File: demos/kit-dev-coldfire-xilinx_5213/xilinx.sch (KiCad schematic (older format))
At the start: 21 parts, among them P1 CONN_6, P3 CONN_2X2, P4 CONN_20X2, U9 XCR3256-TQ144

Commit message: 3d viewer: minor code cleaning (remove useless #include ) dialog_track_via_size: set minimal size  and make dialog resizable. Update demo file.
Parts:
- C51, C52, C53, C54, C55, C56, C57, C58, C59, C60, C61, R57, R62, R63: footprint (none) -> lib_smd:SM0805
- D8, D9: footprint (none) -> lib_smd:SM1206POL
- P1: footprint (none) -> pin_array:PIN_ARRAY-6X1
- P3: footprint (none) -> pin_array:PIN_ARRAY_2X2
- P4: footprint (none) -> pin_array:PIN_ARRAY_20X2
- R64: footprint (none) -> discret:R4
- U9: footprint (none) -> lib_smd:TQFP144
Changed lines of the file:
@@
 F 0 "R64" V 10530 3900 50  0000 C CNN
 F 1 "3,3" V 10450 3900 50  0000 C CNN
-F 2 "" H 10450 3900 60  0001 C CNN
+F 2 "discret:R4" H 10450 3900 60  0001 C CNN
 F 3 "" H 10450 3900 60  0001 C CNN
 	1    10450 3900
@@
 F 0 "P3" H 6600 1400 50  0000 C CNN
 F 1 "CONN_2X2" H 6610 1120 40  0000 C CNN
-F 2 "" H 6600 1250 60  0001 C CNN
+F 2 "pin_array:PIN_ARRAY_2X2" H 6600 1250 60  0001 C CNN
 F 3 "" H 6600 1250 60  0001 C CNN
 	1    6600 1250
@@
 F 0 "U9" H 4600 4150 70  0000 C CNN
 F 1 "XCR3256-TQ144" H 4550 500 60  0000 C CNN
-F 2 "" H 4550 4100 60  0001 C CNN
+F 2 "lib_smd:TQFP144" H 4550 4100 60  0001 C CNN
 F 3 "" H 4550 4100 60  0001 C CNN
 	1    4550 4100
@@
 F 0 "P4" H 9250 3100 60  0000 C CNN
 F 1 "CONN_20X2" V 9200 3050 50  0000 C CNN
-F 2 "" H 9200 3050 60  0001 C CNN
+F 2 "pin_array:PIN_ARRAY_20X2" H 9200 3050 60  0001 C CNN
 F 3 "" H 9200 3050 60  0001 C CNN
 	1    9200 3050
@@
 F 0 "R57" V 3380 650 50  0000 C CNN
 F 1 "4K7" V 3300 650 50  0000 C CNN
-F 2 "" H 3300 650 60  0001 C CNN
+F 2 "lib_smd:SM0805" H 3300 650 60  0001 C CNN
 F 3 "" H 3300 650 60  0001 C CNN
 	1    3300 650
@@
 F 0 "D8" H 9300 5050 50  0000 C CNN
 F 1 "LED" H 9300 4850 50  0000 C CNN
-F 2 "" H 9300 4950 60  0001 C CNN
+F 2 "lib_smd:SM1206POL" H 9300 4950 60  0001 C CNN
 F 3 "" H 9300 4950 60  0001 C CNN
 	1    9300 4950
@@
 F 0 "R62" V 8880 4950 50  0000 C CNN
 F 1 "1K" V 8800 4950 50  0000 C CNN
-F 2 "" H 8800 4950 60  0001 C CNN
+F 2 "lib_smd:SM0805" H 8800 4950 60  0001 C CNN
 F 3 "" H 8800 4950 60  0001 C CNN
 	1    8800 4950
@@
 F 0 "C61" H 10700 6450 50  0000 L CNN
 F 1 "100nF" H 10650 6250 50  0000 L CNN
-F 2 "" H 10650 6350 60  0001 C CNN
+F 2 "lib_smd:SM0805" H 10650 6350 60  0001 C CNN
 F 3 "" H 10650 6350 60  0001 C CNN
 	1    10650 6350
@@
 F 0 "C60" H 10400 6450 50  0000 L CNN
 F 1 "100nF" H 10350 6250 50  0000 L CNN
-F 2 "" H 10350 6350 60  0001 C CNN
+F 2 "lib_smd:SM0805" H 10350 6350 60  0001 C CNN
 F 3 "" H 10350 6350 60  0001 C CNN
 	1    10350 6350
@@
 F 0 "C59" H 10100 6450 50  0000 L CNN
 F 1 "100nF" H 10050 6250 50  0000 L CNN
-F 2 "" H 10050 6350 60  0001 C CNN
+F 2 "lib_smd:SM0805" H 10050 6350 60  0001 C CNN
 F 3 "" H 10050 6350 60  0001 C CNN
 	1    10050 6350
@@
 F 0 "C54" H 8600 6450 50  0000 L CNN
 F 1 "100nF" H 8550 6250 50  0000 L CNN
-F 2 "" H 8550 6350 60  0001 C CNN
+F 2 "lib_smd:SM0805" H 8550 6350 60  0001 C CNN
 F 3 "" H 8550 6350 60  0001 C CNN
 	1    8550 6350
@@
 F 0 "C53" H 8300 6450 50  0000 L CNN
 F 1 "100nF" H 8250 6250 50  0000 L CNN
-F 2 "" H 8250 6350 60  0001 C CNN
+F 2 "lib_smd:SM0805" H 8250 6350 60  0001 C CNN
 F 3 "" H 8250 6350 60  0001 C CNN
 	1    8250 6350
@@
 F 0 "C52" H 8000 6450 50  0000 L CNN
 F 1 "100nF" H 7950 6250 50  0000 L CNN
-F 2 "" H 7950 6350 60  0001 C CNN
+F 2 "lib_smd:SM0805" H 7950 6350 60  0001 C CNN
 F 3 "" H 7950 6350 60  0001 C CNN
 	1    7950 6350
@@
 F 0 "C51" H 7700 6450 50  0000 L CNN
 F 1 "100nF" H 7650 6250 50  0000 L CNN
-F 2 "" H 7650 6350 60  0001 C CNN
+F 2 "lib_smd:SM0805" H 7650 6350 60  0001 C CNN
 F 3 "" H 7650 6350 60  0001 C CNN
 	1    7650 6350
@@
 F 0 "C58" H 9800 6450 50  0000 L CNN
 F 1 "100nF" H 9750 6250 50  0000 L CNN
-F 2 "" H 9750 6350 60  0001 C CNN
+F 2 "lib_smd:SM0805" H 9750 6350 60  0001 C CNN
 F 3 "" H 9750 6350 60  0001 C CNN
 	1    9750 6350
@@
 F 0 "C57" H 9500 6450 50  0000 L CNN
 F 1 "100nF" H 9450 6250 50  0000 L CNN
-F 2 "" H 9450 6350 60  0001 C CNN
+F 2 "lib_smd:SM0805" H 9450 6350 60  0001 C CNN
 F 3 "" H 9450 6350 60  0001 C CNN
 	1    9450 6350
@@
 F 0 "C56" H 9200 6450 50  0000 L CNN
 F 1 "100nF" H 9150 6250 50  0000 L CNN
-F 2 "" H 9150 6350 60  0001 C CNN
+F 2 "lib_smd:SM0805" H 9150 6350 60  0001 C CNN
 F 3 "" H 9150 6350 60  0001 C CNN
 	1    9150 6350
@@
 F 0 "C55" H 8900 6450 50  0000 L CNN
 F 1 "100nF" H 8850 6250 50  0000 L CNN
-F 2 "" H 8850 6350 60  0001 C CNN
+F 2 "lib_smd:SM0805" H 8850 6350 60  0001 C CNN
 F 3 "" H 8850 6350 60  0001 C CNN
 	1    8850 6350
@@
 F 0 "D9" H 9300 5350 50  0000 C CNN
 F 1 "LED" H 9300 5150 50  0000 C CNN
-F 2 "" H 9300 5250 60  0001 C CNN
+F 2 "lib_smd:SM1206POL" H 9300 5250 60  0001 C CNN
 F 3 "" H 9300 5250 60  0001 C CNN
 	1    9300 5250
@@
 F 0 "R63" V 8880 5250 50  0000 C CNN
 F 1 "1K" V 8800 5250 50  0000 C CNN
-F 2 "" H 8800 5250 60  0001 C CNN
+F 2 "lib_smd:SM0805" H 8800 5250 60  0001 C CNN
 F 3 "" H 8800 5250 60  0001 C CNN
 	1    8800 5250
@@
 F 0 "P1" V 2300 1050 60  0000 C CNN
 F 1 "CONN_6" V 2400 1050 60  0000 C CNN
-F 2 "" H 2350 1050 60  0001 C CNN
+F 2 "pin_array:PIN_ARRAY-6X1" H 2350 1050 60  0001 C CNN
 F 3 "" H 2350 1050 60  0001 C CNN
 	1    2350 1050

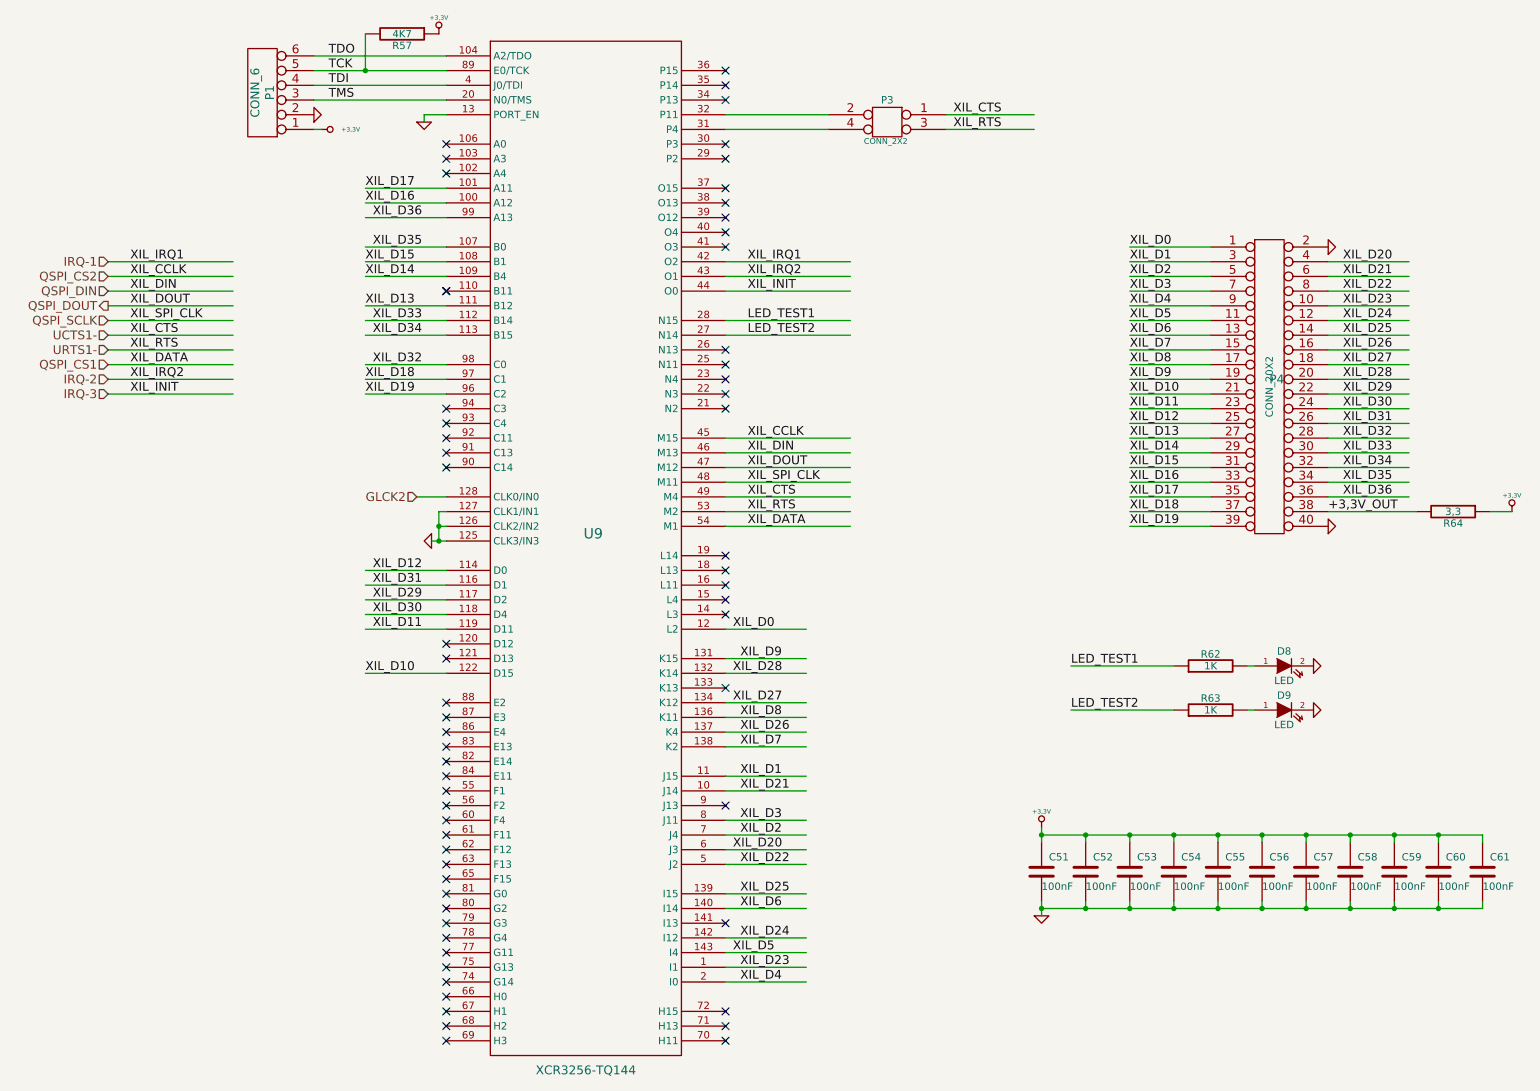
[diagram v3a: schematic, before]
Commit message: demos/ schematic tidying
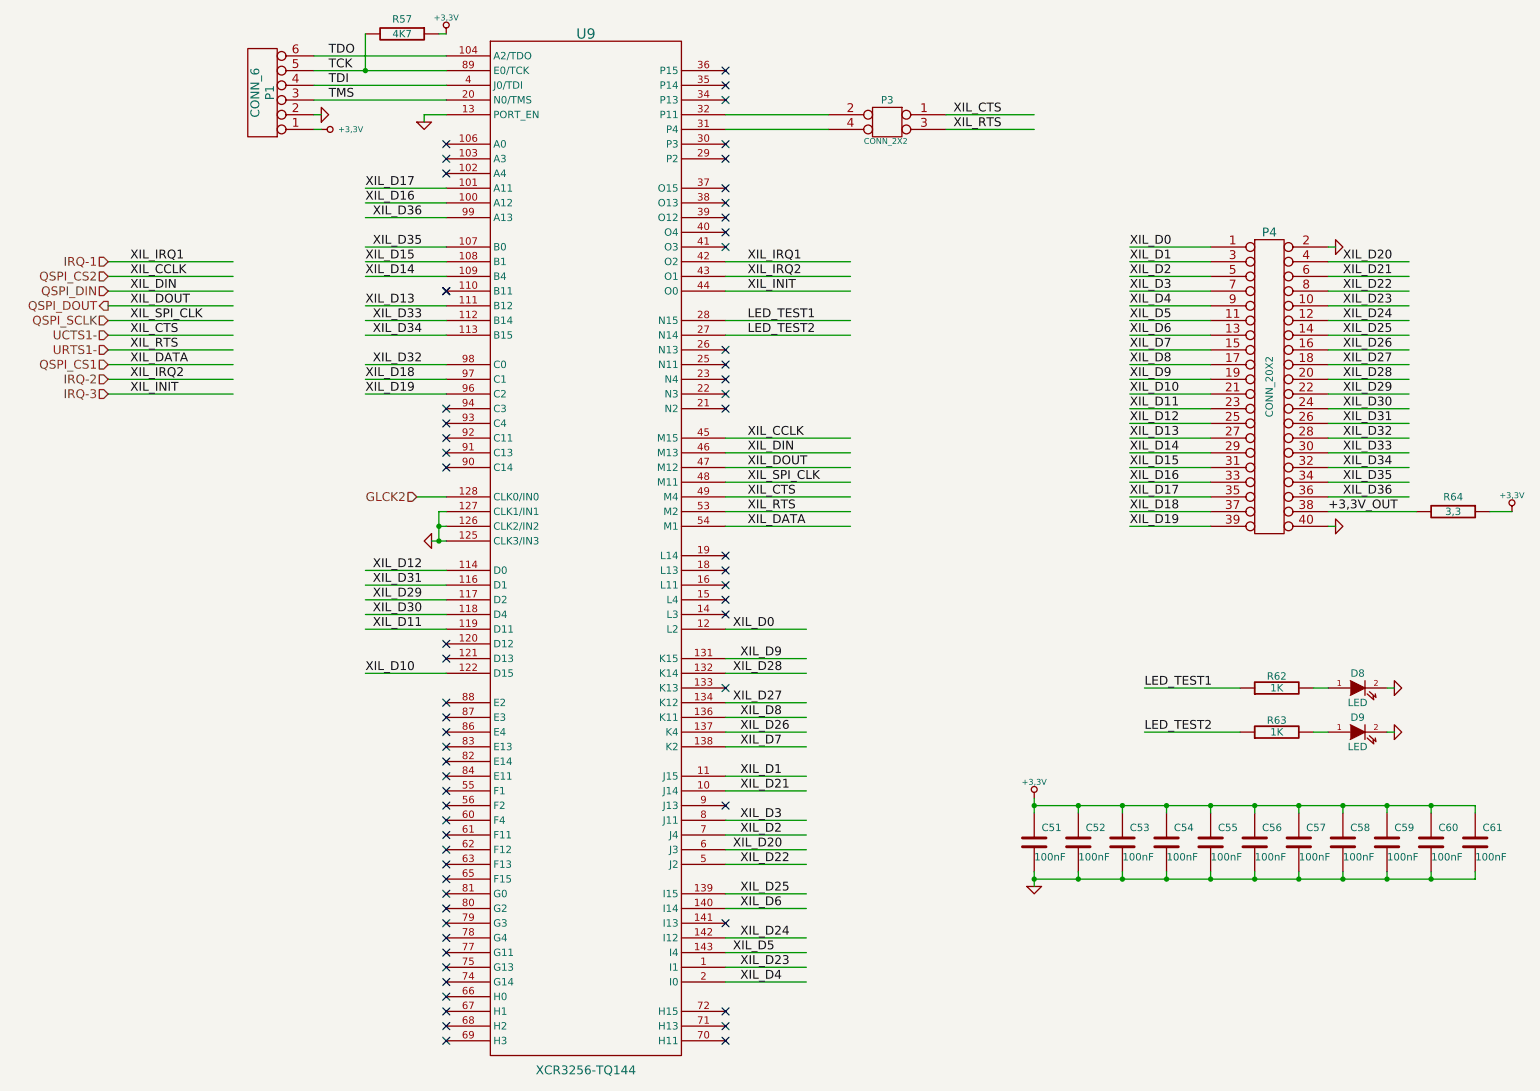
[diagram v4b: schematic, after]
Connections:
- wire segments 143 -> 172
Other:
- moved on the sheet: C51, C52, C53, C54, C55, C56, C57, C58, C59, C60, C61, D8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
